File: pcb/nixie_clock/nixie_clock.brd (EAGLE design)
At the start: 130 x 102 mm, 147 parts, among them J1 USB-C, J2 8, J3 8, J4 4, J5 4, Q1 IRLR3110ZPBF, Q2 BC817-25, Q3 BC817-25, Q4 BC817-25, Q5 BC817-25, Q6 BC817-25, Q7 BC817-25, T1 DA2032-AL, U1 ESP32, U10 74LVC1G17, U11 74LVC1G17, U2 CP2102N, U3 LT3757, U4 DS3231, U5 HV5522, U6 HV5522, U7 MIC39100, U8 W25Q40BVSS, U9 MIC2619, X1 32.768kHz, X2 26MHz

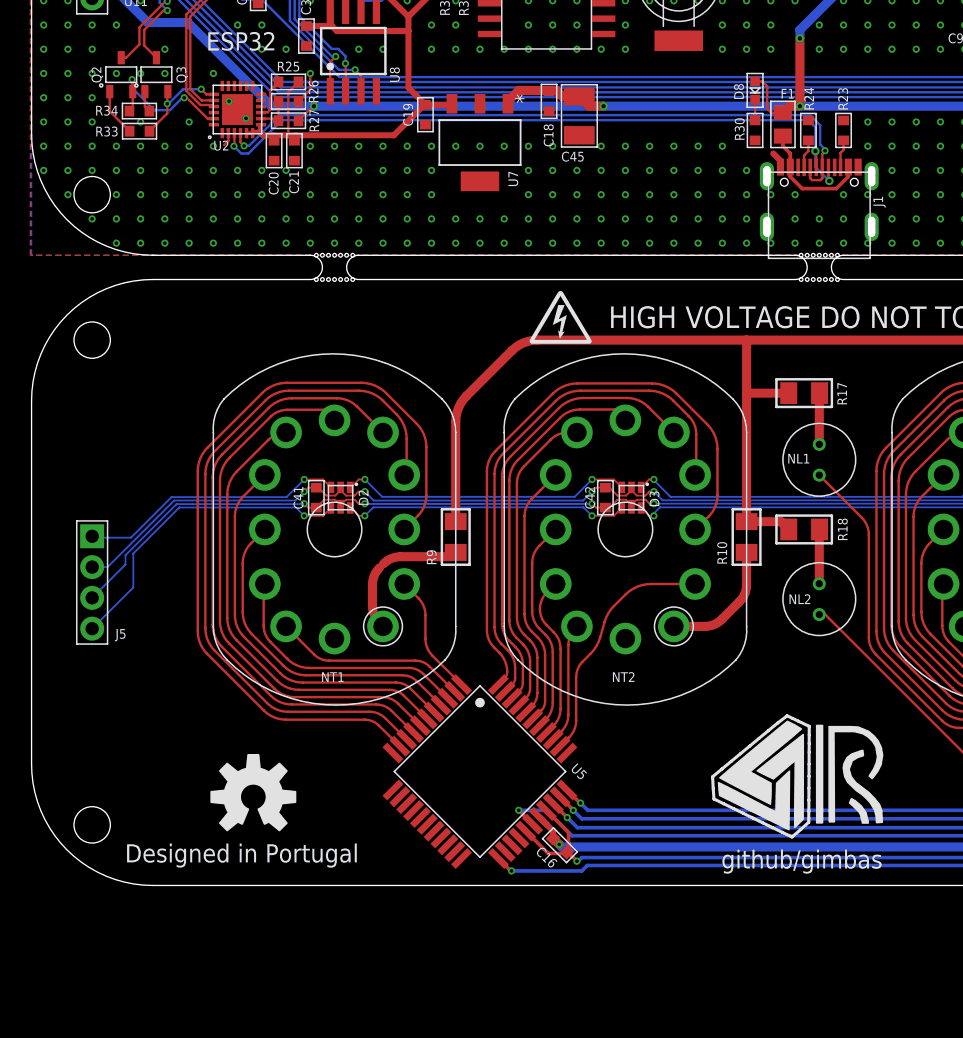
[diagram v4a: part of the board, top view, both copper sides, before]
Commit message: changed usb connector
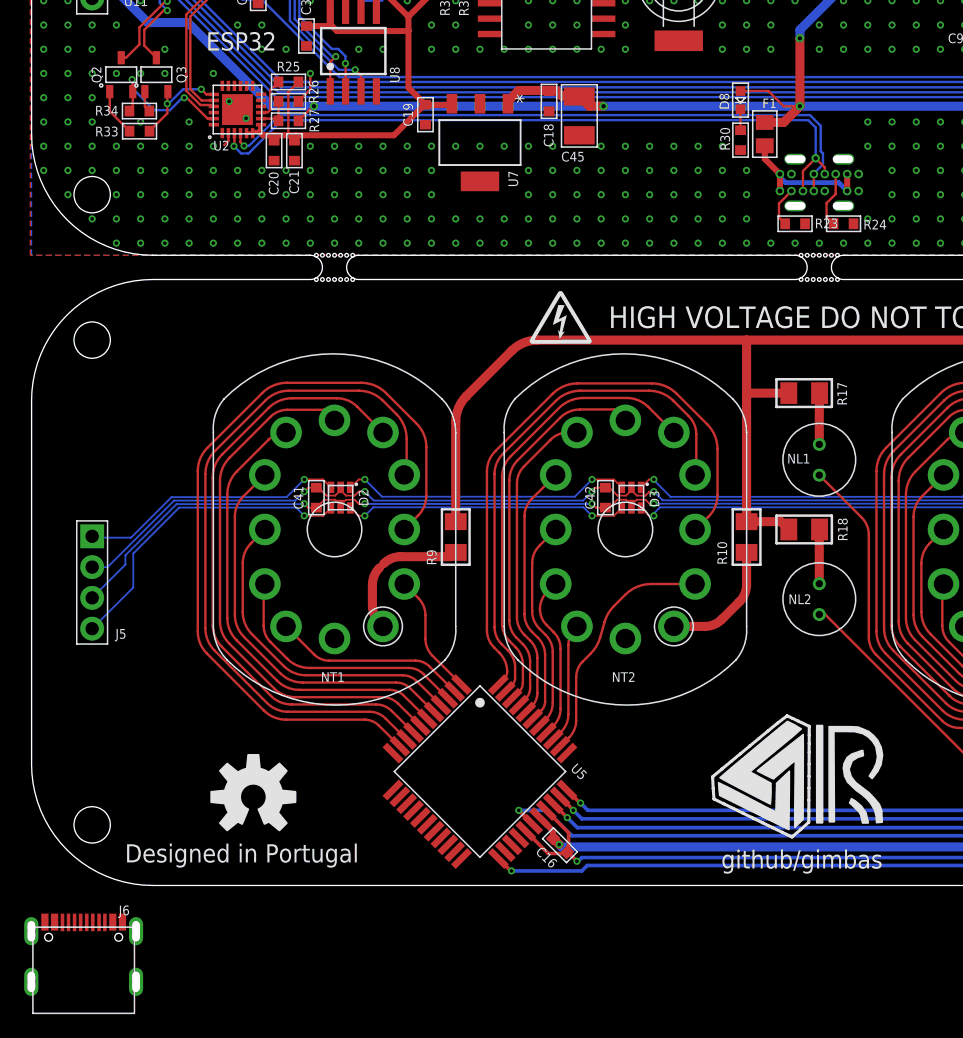
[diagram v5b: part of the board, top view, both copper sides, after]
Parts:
- added J6: USB-C, Connectors > USB:USB-C
- J1: value USB-C -> USB-CVERTICAL; device Connectors > USB:USB-C -> Connectors > USB:USB-C-V
- moved R23 8.68 mm to (63.0, 54.6), turned to 180 degrees
- moved R24 8.23 mm to (67.0, 54.6), turned to 180 degrees
- moved J1 6.00 mm to (65.0, 58.0), flipped to the bottom
- moved F1 1.70 mm to (60.5, 62.0)
- moved D8 1.44 mm to (58.5, 64.8)
- moved R30 1.44 mm to (58.5, 61.5)
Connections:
- net GND: now also J1.A1, J1.B12; no longer J1.A1/B12, J1.B1/A12
- net N$74: now also J1.A4, J1.A9, J1.B4, J1.B9; no longer J1.A4/B9, J1.B4/A9
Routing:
- net 5V: track 189.7 -> 192.5 mm
- net N$78: track 2.37 -> 4.65 mm
- net N$74: track 10.00 -> 11.9 mm
- net GND: track 37.1 -> 35.7 mm, vias 792 -> 786
- net N$75: track 2.33 -> 3.33 mm
- net USB_DM: track 56.8 -> 55.9 mm, vias 2 -> 1
- net USB_DP: track 58.2 -> 58.0 mm, vias 3 -> 2

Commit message: corrected usb pd resistor values
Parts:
- F1: value (none) -> 500mA
- R23, R24: value 11k5 -> 5k11
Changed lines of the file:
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@@
 <?xml version="1.0" encoding="utf-8"?>
 <!DOCTYPE eagle SYSTEM "eagle.dtd">
-<eagle version="9.5.2">
+<eagle version="9.5.1">
 <drawing>
 <settings>
-<setting alwaysvectorfont="yes"/>
+<setting alwaysvectorfont="no"/>
 <setting verticaltext="up"/>
 </settings>
@@
 <attribute name="NAME" x="60.536" y="62.91" size="0.8" layer="22" font="vector" ratio="15" rot="MR270"/>
 </element>
-<element name="F1" library="Circuit Protection &gt; Resettable Fuses - PPTC" package="0805" value="" x="60.5" y="62" smashed="yes" rot="R270">
+<element name="F1" library="Circuit Protection &gt; Resettable Fuses - PPTC" package="0805" value="500mA" x="60.5" y="62" smashed="yes" rot="R270">
 <attribute name="NAME" x="60.8932" y="64.5288" size="0.8" layer="25" font="vector" ratio="12" rot="SR0" align="center"/>
 <attribute name="VALUE" x="56.9376" y="65.5306" size="2.0828" layer="27" ratio="10" rot="SR270"/>
 </element>
-<element name="R23" library="Passive Components &gt; Resistors &gt; Chip Resistors" package="0603_WAVE" value="11k5" x="63" y="54.6" smashed="yes" rot="R180">
+<element name="R23" library="Passive Components &gt; Resistors &gt; Chip Resistors" package="0603_WAVE" value="5k11" x="63" y="54.6" smashed="yes" rot="R180">
 <attribute name="NAME" x="65.6" y="54.63" size="0.8" layer="25" font="vector" ratio="12" rot="R180" align="center"/>
 </element>
-<element name="R24" library="Passive Components &gt; Resistors &gt; Chip Resistors" package="0603_WAVE" value="11k5" x="67" y="54.6" smashed="yes" rot="R180">
+<element name="R24" library="Passive Components &gt; Resistors &gt; Chip Resistors" package="0603_WAVE" value="5k11" x="67" y="54.6" smashed="yes" rot="R180">
 <attribute name="NAME" x="69.6" y="54.53" size="0.8" layer="25" font="vector" ratio="12" rot="R180" align="center"/>
 </element>
